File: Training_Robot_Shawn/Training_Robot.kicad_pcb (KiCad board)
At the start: 2 copper layers, 87.5 x 91.5 mm, 26 parts, among them J1 Conn_01x04_Pin, J2 Conn_01x04_Pin, J3 Conn_01x04_Pin, J6 Conn_01x08_Socket, M1 FrontL, M2 FrontR, M3 BackL, M4 BackR, SW1 SW_SPDT_312, U3 ESP32-S3-DevKitC

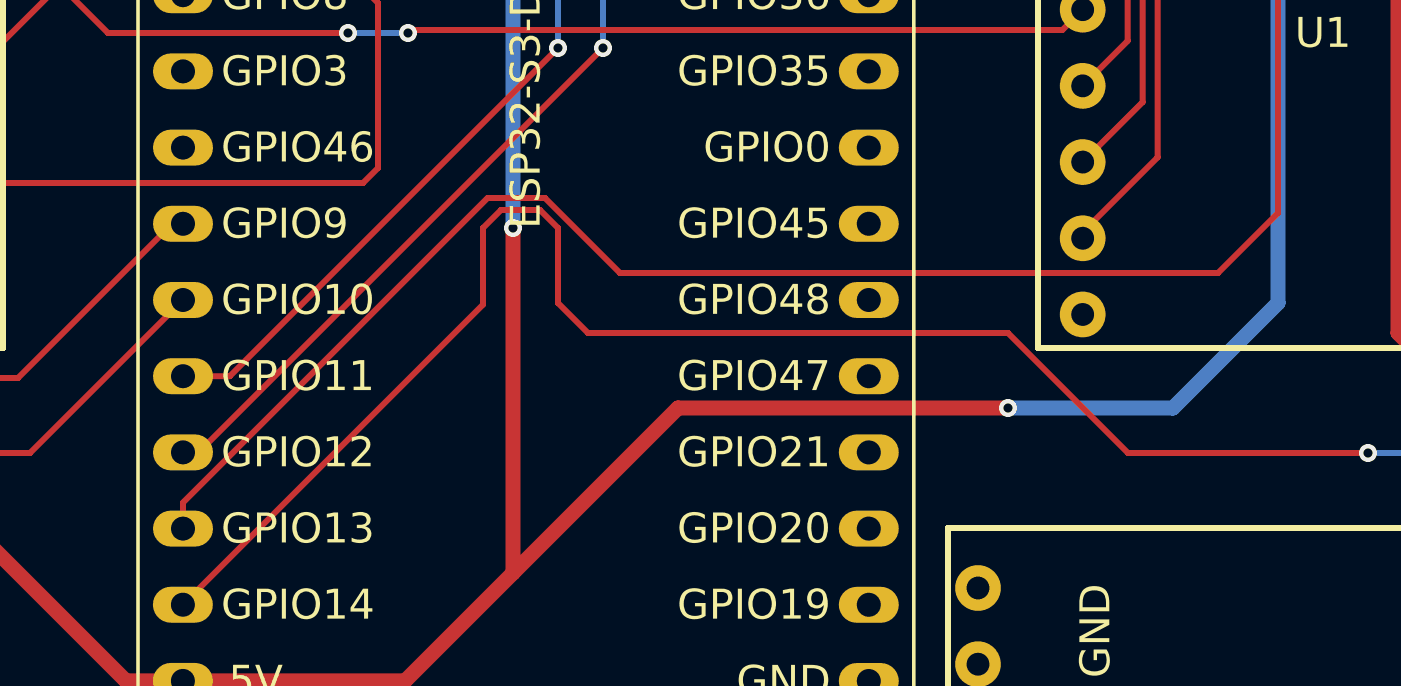
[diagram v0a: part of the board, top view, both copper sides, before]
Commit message: schematic changes made
-removed r1
-reduced r2 to 180 ohms
-added fuses for motor drivers
-removed usb pd module and added symbols for xt60 (battery), buck converter, and block terminal (5v)
-only missing fuse footprints
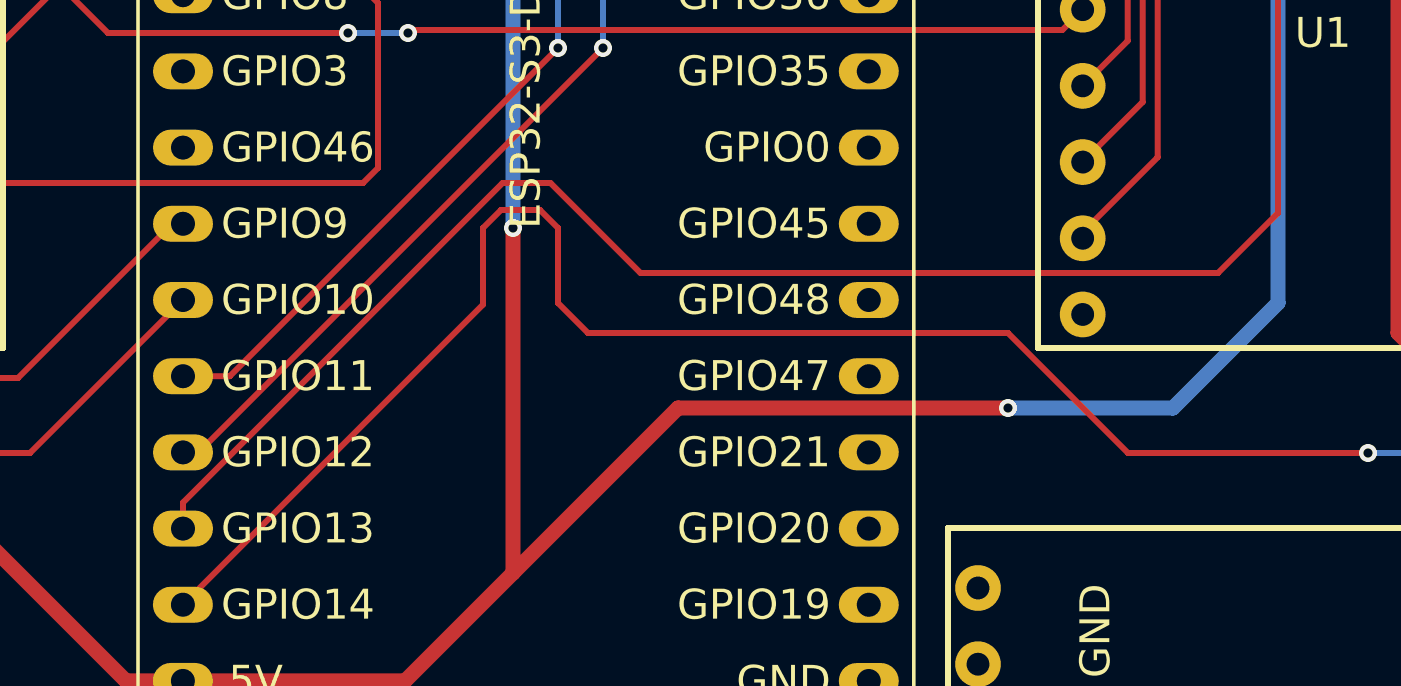
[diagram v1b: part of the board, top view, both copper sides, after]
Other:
- copper layers 2 -> 4
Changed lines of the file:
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@@
 	(layers
 		(0 "F.Cu" signal)
+		(4 "In1.Cu" signal)
+		(6 "In2.Cu" signal)
 		(2 "B.Cu" signal)
 		(9 "F.Adhes" user "F.Adhesive")
@@
 	)
 	(setup
+		(stackup
+			(layer "F.SilkS"
+				(type "Top Silk Screen")
+			)
+			(layer "F.Paste"
+				(type "Top Solder Paste")
+			)
+			(layer "F.Mask"
+				(type "Top Solder Mask")
+				(thickness 0.01)
+			)
+			(layer "F.Cu"
+				(type "copper")
+				(thickness 0.035)
+			)
+			(layer "dielectric 1"
+				(type "prepreg")
+				(thickness 0.1)
+				(material "FR4")
+				(epsilon_r 4.5)
+				(loss_tangent 0.02)
+			)
+			(layer "In1.Cu"
+				(type "copper")
+				(thickness 0.035)
+			)
+			(layer "dielectric 2"
+				(type "core")
+				(thickness 1.24)
+				(material "FR4")
+				(epsilon_r 4.5)
+				(loss_tangent 0.02)
+			)
+			(layer "In2.Cu"
+				(type "copper")
+				(thickness 0.035)
+			)
+			(layer "dielectric 3"
+				(type "prepreg")
+				(thickness 0.1)
+				(material "FR4")
+				(epsilon_r 4.5)
+				(loss_tangent 0.02)
+			)
+			(layer "B.Cu"
+				(type "copper")
+				(thickness 0.035)
+			)
+			(layer "B.Mask"
+				(type "Bottom Solder Mask")
+				(thickness 0.01)
+			)
+			(layer "B.Paste"
+				(type "Bottom Solder Paste")
+			)
+			(layer "B.SilkS"
+				(type "Bottom Silk Screen")
+			)
+			(copper_finish "None")
+			(dielectric_constraints no)
+		)
 		(pad_to_mask_clearance 0)
 		(allow_soldermask_bridges_in_footprints no)
@@
 		(capping no)
 		(filling no)
+		(zone_defaults)
 		(pcbplotparams
 			(layerselection 0x00000000_00000000_55555555_575555ff)
@@
 	)
 	(segment
-		(start 96.065685 94)
-		(end 94.152792 94)
+		(start 125.75 70.5)
+		(end 122.25 70.5)
 		(width 0.2)
 		(layer "F.Cu")
@@
 	)
 	(segment
-		(start 120.5 94.5)
-		(end 118.5 96.5)
+		(start 84 104.152792)
+		(end 84 105.02)
 		(width 0.2)
 		(layer "F.Cu")
@@
 	)
 	(segment
-		(start 122.25 70.5)
-		(end 120.5 72.25)
+		(start 99.25 96.5)
+		(end 96.25 93.5)
 		(width 0.2)
 		(layer "F.Cu")
@@
 	)
 	(segment
-		(start 125.75 70.5)
-		(end 122.25 70.5)
+		(start 120.5 72.25)
+		(end 120.5 94.5)
 		(width 0.2)
 		(layer "F.Cu")
@@
 	)
 	(segment
-		(start 118.5 96.5)
-		(end 98.565685 96.5)
+		(start 96.25 93.5)
+		(end 94.652792 93.5)
 		(width 0.2)
 		(layer "F.Cu")
@@
 	)
 	(segment
-		(start 120.5 72.25)
-		(end 120.5 94.5)
+		(start 94.652792 93.5)
+		(end 84 104.152792)
 		(width 0.2)
 		(layer "F.Cu")
@@
 	)
 	(segment
-		(start 84 104.152792)
-		(end 84 105.02)
+		(start 120.5 94.5)
+		(end 118.5 96.5)
 		(width 0.2)
 		(layer "F.Cu")
@@
 	)
 	(segment
-		(start 94.152792 94)
-		(end 84 104.152792)
+		(start 122.25 70.5)
+		(end 120.5 72.25)
 		(width 0.2)
 		(layer "F.Cu")
@@
 	)
 	(segment
-		(start 98.565685 96.5)
-		(end 96.065685 94)
+		(start 118.5 96.5)
+		(end 99.25 96.5)
 		(width 0.2)
 		(layer "F.Cu")
@@
 	)
 	(segment
-		(start 94 95)
-		(end 94 97.5536)
-		(width 0.2)
-		(layer "F.Cu")
-		(net "/R_US_ECHO")
-	)
-	(segment
-		(start 96.5 95)
-		(end 95.9 94.4)
+		(start 96.5 97.5)
+		(end 96.5 95)
 		(width 0.2)
 		(layer "F.Cu")
@@
 	)
 	(segment
-		(start 94.6 94.4)
-		(end 94 95)
+		(start 95.9 94.4)
+		(end 94.6 94.4)
 		(width 0.2)
 		(layer "F.Cu")
@@
 	)
 	(segment
-		(start 96.5 97.5)
-		(end 96.5 95)
+		(start 111.5 98.5)
+		(end 97.5 98.5)
 		(width 0.2)
 		(layer "F.Cu")
@@
 	)
 	(segment
-		(start 111.5 98.5)
-		(end 97.5 98.5)
+		(start 94.6 94.4)
+		(end 94 95)
 		(width 0.2)
 		(layer "F.Cu")
@@
 	)
 	(segment
-		(start 123.5 102.5)
-		(end 115.5 102.5)
+		(start 94 97.5536)
+		(end 83.99632 107.55728)
 		(width 0.2)
 		(layer "F.Cu")
@@
 	)
 	(segment
-		(start 135.5 85.04)
-		(end 133 87.54)
+		(start 96.5 95)
+		(end 95.9 94.4)
 		(width 0.2)
 		(layer "F.Cu")
@@
 	)
 	(segment
-		(start 95.9 94.4)
-		(end 94.6 94.4)
+		(start 123.5 102.5)
+		(end 115.5 102.5)
 		(width 0.2)
 		(layer "F.Cu")
@@
 	)
 	(segment
-		(start 94 97.5536)
-		(end 83.99632 107.55728)
+		(start 97.5 98.5)
+		(end 96.5 97.5)
 		(width 0.2)
 		(layer "F.Cu")
@@
 	)
 	(segment
-		(start 97.5 98.5)
-		(end 96.5 97.5)
+		(start 94 95)
+		(end 94 97.5536)
+		(width 0.2)
+		(layer "F.Cu")
+		(net "/R_US_ECHO")
+	)
+	(segment
+		(start 135.5 85.04)
+		(end 133 87.54)
 		(width 0.2)
 		(layer "F.Cu")

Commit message: add uncompleted layout
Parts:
- removed R1: 10K, Resistor_THT:R_Axial_DIN0204_L3.6mm_D1.6mm_P5.08mm_Horizontal
- removed U1, U2: ~, MARS Custom Footprints:TB6612FNG Breakout
- removed U4: ~, MARS Custom Footprints:USB PD Module
- added H5: MountingHole, MountingHole:MountingHole_4.5mm, F.Cu at (123.2, 94.0)
- added J5: Conn_01x02_Pin, TerminalBlock_Phoenix:TerminalBlock_Phoenix_MKDS-1,5-2_1x02_P5.00mm_Horizontal, F.Cu at (120.7, 114.3)
- R2: value 10K -> 180; footprint Resistor_THT:R_Axial_DIN0204_L3.6mm_D1.6mm_P5.08mm_Horizontal -> Resistor_THT:R_Axial_DIN0204_L3.6mm_D1.6mm_P7.62mm_Horizontal
- R3, R4, R5, R6, R7, R8: footprint Resistor_THT:R_Axial_DIN0204_L3.6mm_D1.6mm_P5.08mm_Horizontal -> Resistor_THT:R_Axial_DIN0204_L3.6mm_D1.6mm_P7.62mm_Horizontal
- U3: footprint PCM_Espressif:ESP32-S3-DevKitC -> Espressif:ESP32-S3-DevKitC
- moved U3 62.0 mm to (114.3, 113.4), turned to 180 degrees
- moved J6 47.0 mm to (87.5, 95.6), turned to 180 degrees
- moved D1 20.3 mm to (90.0, 35.0)
- moved R2 20.2 mm to (79.7, 35.0), turned to 0 degrees
- moved M3 11.6 mm to (63.5, 95.2)
- moved M4 10.7 mm to (139.7, 101.6)
- moved H3 10.3 mm to (63.5, 114.3)
- moved R5 10.1 mm to (103.8, 41.7), turned to -90 degrees
- moved SW1 10.0 mm to (91.2, 45.1)
- moved H4 10.0 mm to (139.7, 114.3)
- moved J2 9.72 mm to (98.8, 36.5)
- moved R8 9.49 mm to (129.6, 80.5), turned to 0 degrees
- moved H2 7.83 mm to (139.7, 38.1)
- moved H1 6.94 mm to (63.5, 38.1)
- moved R3 6.56 mm to (65.6, 75.5)
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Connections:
- D1 pad 2: Net-(D1-A) -> /STBY
- SW1 pad 1: Net-(D1-A) -> /STBY
- U3 pad 21: +5V -> unconnected-(U3-5V-Pad21)
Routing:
- net +5V: track 210.2 -> 0.00 mm, vias 6 -> 0
- net +12V: track 110.4 -> 0.00 mm
- net /STBY: track 73.5 -> 11.4 mm, vias 4 -> 0
- net /R_US_ECHO: track 81.0 -> 27.8 mm, vias 2 -> 0
- net /RIGHT_FORWARD: track 49.5 -> 0.00 mm
- net /RIGHT_BACKWARD: track 49.2 -> 0.00 mm
- net /FL+: track 48.4 -> 0.00 mm
- net /BL+: track 44.9 -> 0.00 mm
- net /FL-: track 43.4 -> 0.00 mm
- net /FR-: track 40.2 -> 0.00 mm
- net /RIGHT_EN: track 39.0 -> 0.00 mm
- net /L_US_TRIG: track 45.9 -> 83.8 mm, vias 2 -> 0
- net /R_US_TRIG: track 85.6 -> 49.4 mm, vias 2 -> 0
- net /LEFT_FORWARD: track 35.0 -> 0.00 mm
- net /F_US_ECHO: track 64.1 -> 32.5 mm, vias 2 -> 0
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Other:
- board size 87.5 x 91.5 mm -> 88.9 x 88.9 mm

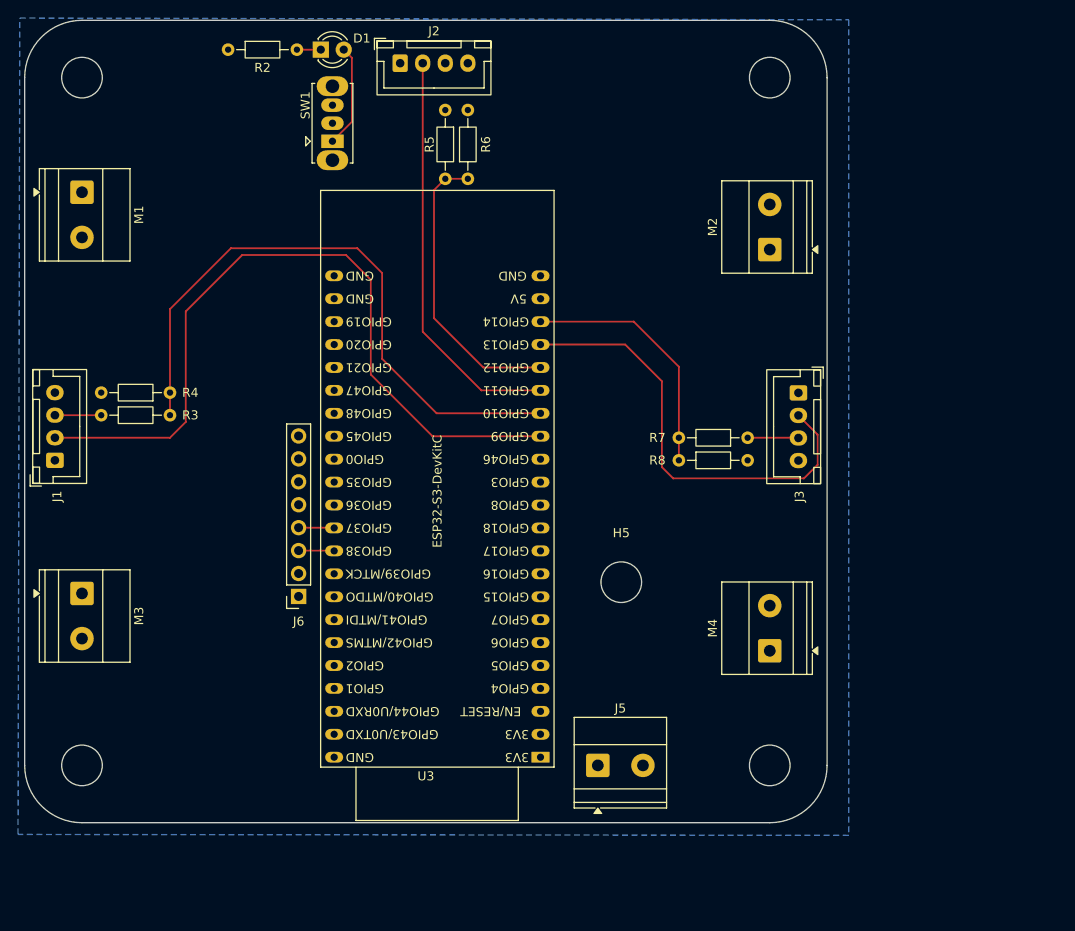
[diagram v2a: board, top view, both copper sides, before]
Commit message: add all components except for buck converter
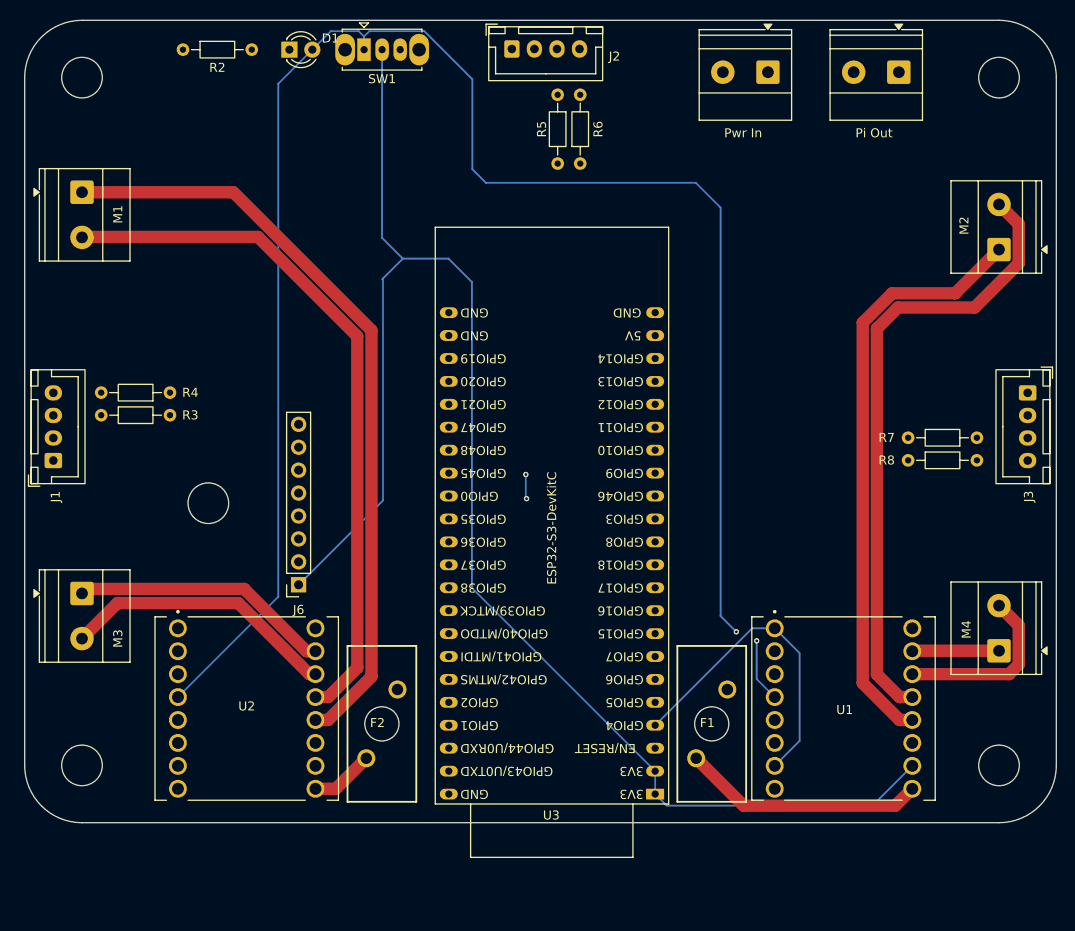
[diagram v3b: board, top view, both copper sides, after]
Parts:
- added F1: Fuse, 01530008Z:01530008, F.Cu at (133.3, 109.7)
- added F2: Fuse, 01530008Z:01530008, F.Cu at (96.7, 109.7)
- added Pwr In: Conn_01x02_Pin, TerminalBlock_Phoenix:TerminalBlock_Phoenix_MKDS-1,5-2_1x02_P5.00mm_Horizontal, F.Cu at (139.5, 37.5)
- added U1: ~, ROB-14450:MODULE_ROB-14450, F.Cu at (147.9, 108.0)
- added U2: ~, ROB-14450:MODULE_ROB-14450, F.Cu at (81.8, 108.0)
- Pi Out: renamed from J5
- moved Pi Out 83.7 mm to (154.0, 37.5), turned to 180 degrees
- moved H5 46.6 mm to (77.5, 85.2)
- moved H2 25.4 mm to (165.1, 38.1)
- moved H4 25.4 mm to (165.1, 114.3)
- moved J3 25.4 mm to (168.3, 73.0)
- moved M2 25.4 mm to (165.1, 57.1)
- moved M4 25.4 mm to (165.1, 101.6)
- moved R7 25.4 mm to (162.7, 78.0)
- moved R8 25.4 mm to (155.0, 80.5)
- moved U3 13.3 mm to (127.0, 117.5)
- moved R5 12.6 mm to (116.2, 40.0)
- moved R6 12.6 mm to (118.7, 47.6)
- moved J2 12.5 mm to (111.1, 34.9)
- moved SW1 10.7 mm to (94.8, 35.0), turned to 0 degrees
- moved R2 5.00 mm to (74.7, 35.0)
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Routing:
- net /STBY: track 11.4 -> 197.3 mm, vias 0 -> 2
- net +5V: track 0.00 -> 183.1 mm
- net /LEFT_FORWARD: track 0.00 -> 126.9 mm
- net /LEFT_EN: track 0.00 -> 119.4 mm, vias 0 -> 2
- net /LEFT_BACKWARD: track 0.00 -> 117.8 mm
- net /FL+: track 0.00 -> 85.0 mm
- net /FL-: track 0.00 -> 77.8 mm
- net /FR-: track 0.00 -> 69.4 mm
- net /FR+: track 0.00 -> 65.6 mm
- net +3V3: track 124.7 -> 169.9 mm
- net /RIGHT_EN: track 0.00 -> 35.2 mm
- net /BL-: track 0.00 -> 30.8 mm
- net /BL+: track 0.00 -> 28.9 mm
- net Net-(U1-VM): track 0.00 -> 26.9 mm
- net /RIGHT_BACKWARD: track 0.00 -> 26.1 mm
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- added copper zone on In1.Cu, net GND
- removed copper zone on B.Cu, net GND
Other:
- board size 88.9 x 88.9 mm -> 114.3 x 88.9 mm
